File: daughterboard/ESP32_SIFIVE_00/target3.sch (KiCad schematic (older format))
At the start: 21 parts, among them IC2 W25X40CLSNIG, U3 ESP32-C3

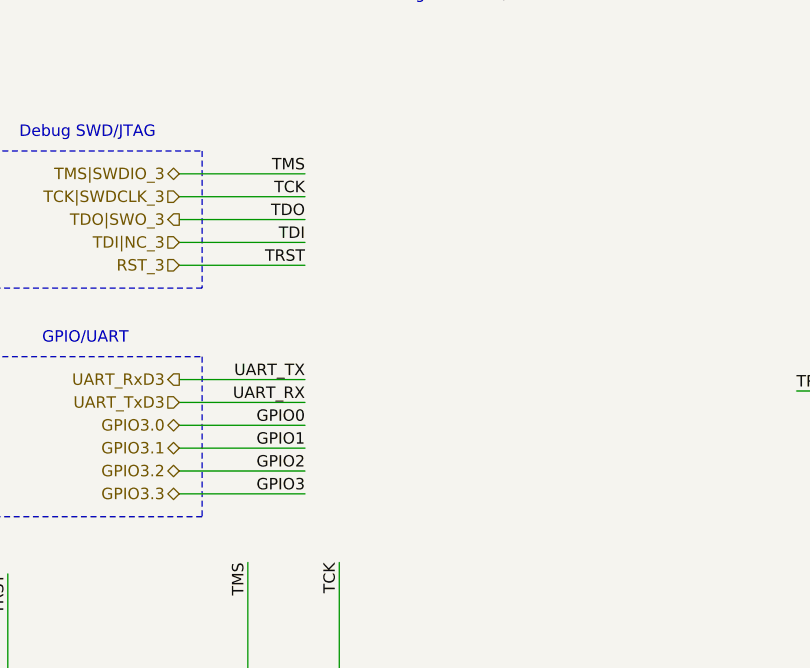
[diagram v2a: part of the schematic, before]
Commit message: added testpoints to daughterboards, updated readme
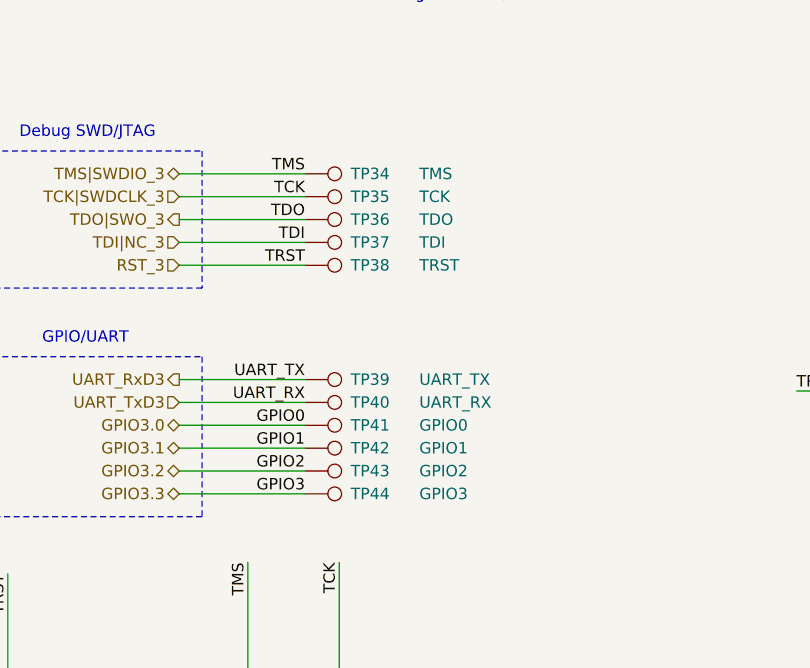
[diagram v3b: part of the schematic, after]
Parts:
- added TP34: TMS, symbol Connector:TestPoint
- added TP35: TCK, symbol Connector:TestPoint
- added TP36: TDO, symbol Connector:TestPoint
- added TP37: TDI, symbol Connector:TestPoint
- added TP38: TRST, symbol Connector:TestPoint
- added TP39: UART_TX, symbol Connector:TestPoint
- added TP40: UART_RX, symbol Connector:TestPoint
- added TP41: GPIO0, symbol Connector:TestPoint
- added TP42: GPIO1, symbol Connector:TestPoint
- added TP43: GPIO2, symbol Connector:TestPoint
- added TP44: GPIO3, symbol Connector:TestPoint
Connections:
- net GPIO3.0: now also TP41.1
- net GPIO3.1: now also TP42.1
- net GPIO3.2: now also TP43.1
- net GPIO3.3: now also TP44.1
- net RST_3: now also TP38.1
- net TCK|SWDCLK_3: now also TP35.1
- net TDI|NC_3: now also TP37.1
- net TDO|SWO_3: now also TP36.1
- net TMS|SWDIO_3: now also TP34.1
- net UART_RxD3: now also TP39.1
- net UART_TxD3: now also TP40.1
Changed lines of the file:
@@
+	0    1    1    0
+$EndComp
+$Comp
+L Connector:TestPoint TP?
+U 1 1 6191A87B
+P 2200 1700
+AR Path="/616688D6/6191A87B" Ref="TP?"  Part="1"
+AR Path="/61668157/6191A87B" Ref="TP34"  Part="1"
+F 0 "TP34" V 2200 1900 50  0000 L CNN
+F 1 "TMS" V 2200 2200 50  0000 L CNN
+F 2 "" H 2400 1700 50  0001 C CNN
+F 3 "~" H 2400 1700 50  0001 C CNN
+	1    2200 1700
+	0    1    1    0
+$EndComp
+$Comp
+L Connector:TestPoint TP?
+U 1 1 6191A881
+P 2200 1800
+AR Path="/616688D6/6191A881" Ref="TP?"  Part="1"
+AR Path="/61668157/6191A881" Ref="TP35"  Part="1"
+F 0 "TP35" V 2200 2000 50  0000 L CNN
+F 1 "TCK" V 2200 2300 50  0000 L CNN
+F 2 "" H 2400 1800 50  0001 C CNN
+F 3 "~" H 2400 1800 50  0001 C CNN
+	1    2200 1800
+	0    1    1    0
+$EndComp
+$Comp
+L Connector:TestPoint TP?
+U 1 1 6191A887
+P 2200 1900
+AR Path="/616688D6/6191A887" Ref="TP?"  Part="1"
+AR Path="/61668157/6191A887" Ref="TP36"  Part="1"
+F 0 "TP36" V 2200 2100 50  0000 L CNN
+F 1 "TDO" V 2200 2400 50  0000 L CNN
+F 2 "" H 2400 1900 50  0001 C CNN
+F 3 "~" H 2400 1900 50  0001 C CNN
+	1    2200 1900
+	0    1    1    0
+$EndComp
+$Comp
+L Connector:TestPoint TP?
+U 1 1 6191A88D
+P 2200 2000
+AR Path="/616688D6/6191A88D" Ref="TP?"  Part="1"
+AR Path="/61668157/6191A88D" Ref="TP37"  Part="1"
+F 0 "TP37" V 2200 2200 50  0000 L CNN
+F 1 "TDI" V 2200 2500 50  0000 L CNN
+F 2 "" H 2400 2000 50  0001 C CNN
+F 3 "~" H 2400 2000 50  0001 C CNN
+	1    2200 2000
+	0    1    1    0
+$EndComp
+$Comp
+L Connector:TestPoint TP?
+U 1 1 6191A893
+P 2200 2100
+AR Path="/616688D6/6191A893" Ref="TP?"  Part="1"
+AR Path="/61668157/6191A893" Ref="TP38"  Part="1"
+F 0 "TP38" V 2200 2300 50  0000 L CNN
+F 1 "TRST" V 2200 2600 50  0000 L CNN
+F 2 "" H 2400 2100 50  0001 C CNN
+F 3 "~" H 2400 2100 50  0001 C CNN
+	1    2200 2100
+	0    1    1    0
+$EndComp
+$Comp
+L Connector:TestPoint TP?
+U 1 1 6191A899
+P 2200 2600
+AR Path="/616688D6/6191A899" Ref="TP?"  Part="1"
+AR Path="/61668157/6191A899" Ref="TP39"  Part="1"
+F 0 "TP39" V 2200 2800 50  0000 L CNN
+F 1 "UART_TX" V 2200 3100 50  0000 L CNN
+F 2 "" H 2400 2600 50  0001 C CNN
+F 3 "~" H 2400 2600 50  0001 C CNN
+	1    2200 2600
+	0    1    1    0
+$EndComp
+$Comp
+L Connector:TestPoint TP?
+U 1 1 6191A89F
+P 2200 2700
+AR Path="/616688D6/6191A89F" Ref="TP?"  Part="1"
+AR Path="/61668157/6191A89F" Ref="TP40"  Part="1"
+F 0 "TP40" V 2200 2900 50  0000 L CNN
+F 1 "UART_RX" V 2200 3200 50  0000 L CNN
+F 2 "" H 2400 2700 50  0001 C CNN
+F 3 "~" H 2400 2700 50  0001 C CNN
+	1    2200 2700
+	0    1    1    0
+$EndComp
+$Comp
+L Connector:TestPoint TP?
+U 1 1 6191A8A5
+P 2200 2800
+AR Path="/616688D6/6191A8A5" Ref="TP?"  Part="1"
+AR Path="/61668157/6191A8A5" Ref="TP41"  Part="1"
+F 0 "TP41" V 2200 3000 50  0000 L CNN
+F 1 "GPIO0" V 2200 3300 50  0000 L CNN
+F 2 "" H 2400 2800 50  0001 C CNN
+F 3 "~" H 2400 2800 50  0001 C CNN
+	1    2200 2800
+	0    1    1    0
+$EndComp
+$Comp
+L Connector:TestPoint TP?
+U 1 1 6191A8AB
+P 2200 2900
+AR Path="/616688D6/6191A8AB" Ref="TP?"  Part="1"
+AR Path="/61668157/6191A8AB" Ref="TP42"  Part="1"
+F 0 "TP42" V 2200 3100 50  0000 L CNN
+F 1 "GPIO1" V 2200 3400 50  0000 L CNN
+F 2 "" H 2400 2900 50  0001 C CNN
+F 3 "~" H 2400 2900 50  0001 C CNN
+	1    2200 2900
+	0    1    1    0
+$EndComp
+$Comp
+L Connector:TestPoint TP?
+U 1 1 6191A8B1
+P 2200 3000
+AR Path="/616688D6/6191A8B1" Ref="TP?"  Part="1"
+AR Path="/61668157/6191A8B1" Ref="TP43"  Part="1"
+F 0 "TP43" V 2200 3200 50  0000 L CNN
+F 1 "GPIO2" V 2200 3500 50  0000 L CNN
+F 2 "" H 2400 3000 50  0001 C CNN
+F 3 "~" H 2400 3000 50  0001 C CNN
+	1    2200 3000
+	0    1    1    0
+$EndComp
+$Comp
+L Connector:TestPoint TP?
+U 1 1 6191A8B7
+P 2200 3100
+AR Path="/616688D6/6191A8B7" Ref="TP?"  Part="1"
+AR Path="/61668157/6191A8B7" Ref="TP44"  Part="1"
+F 0 "TP44" V 2200 3300 50  0000 L CNN
+F 1 "GPIO3" V 2200 3600 50  0000 L CNN
+F 2 "" H 2400 3100 50  0001 C CNN
+F 3 "~" H 2400 3100 50  0001 C CNN
+	1    2200 3100
 	0    1    1    0
 $EndComp

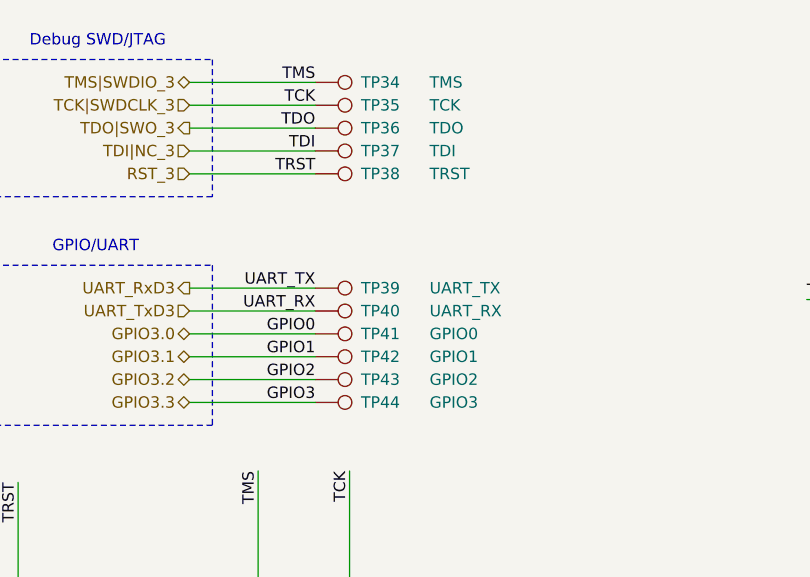
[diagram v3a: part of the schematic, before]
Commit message: started with esp32/sifive layout
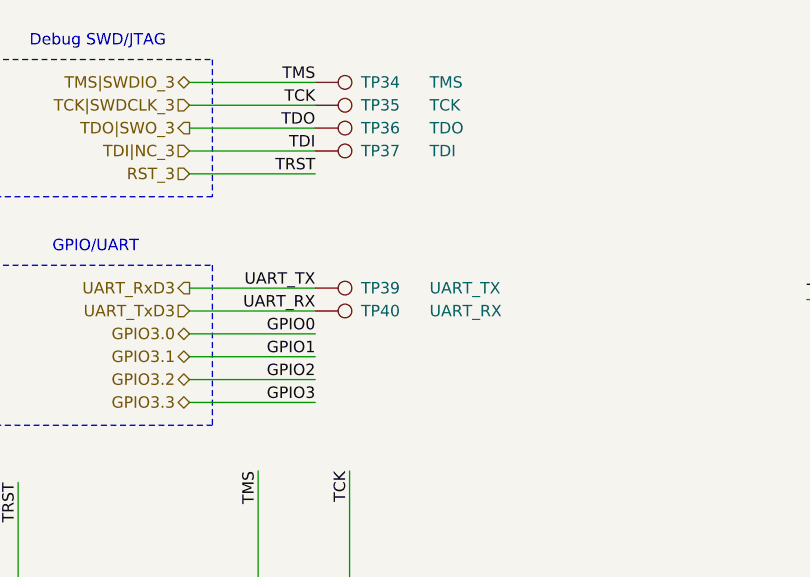
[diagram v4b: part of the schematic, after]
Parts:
- removed TP38: TRST, symbol Connector:TestPoint
- removed TP41: GPIO0, symbol Connector:TestPoint
- removed TP42: GPIO1, symbol Connector:TestPoint
- removed TP43: GPIO2, symbol Connector:TestPoint
- removed TP44: GPIO3, symbol Connector:TestPoint
- C16, C17, C18, C19, C20, C21, C22, C23, C24, C25: footprint (none) -> Capacitor_SMD:C_0603_1608Metric_Pad1.05x0.95mm_HandSolder
- JP4, JP5: footprint (none) -> Jumper:SolderJumper-2_P1.3mm_Open_TrianglePad1.0x1.5mm
- R13, R14, R15, R16, R17, R18, R19: footprint (none) -> Resistor_SMD:R_0603_1608Metric_Pad1.05x0.95mm_HandSolder
- TP34, TP35, TP36, TP37, TP39, TP40: footprint (none) -> TestPoint:TestPoint_Pad_1.0x1.0mm
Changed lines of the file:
@@
 F 0 "C17" H 4792 7046 50  0000 L CNN
 F 1 "1u" H 4792 6955 50  0000 L CNN
-F 2 "" H 4700 7000 50  0001 C CNN
+F 2 "Capacitor_SMD:C_0603_1608Metric_Pad1.05x0.95mm_HandSolder" H 4700 7000 50  0001 C CNN
 F 3 "~" H 4700 7000 50  0001 C CNN
 	1    4700 7000
@@
 F 0 "C18" H 5092 7046 50  0000 L CNN
 F 1 "100n" H 5092 6955 50  0000 L CNN
-F 2 "" H 5000 7000 50  0001 C CNN
+F 2 "Capacitor_SMD:C_0603_1608Metric_Pad1.05x0.95mm_HandSolder" H 5000 7000 50  0001 C CNN
 F 3 "~" H 5000 7000 50  0001 C CNN
 	1    5000 7000
@@
 F 0 "R16" H 5509 6796 50  0000 L CNN
 F 1 "10k" H 5509 6705 50  0000 L CNN
-F 2 "" H 5450 6750 50  0001 C CNN
+F 2 "Resistor_SMD:R_0603_1608Metric_Pad1.05x0.95mm_HandSolder" H 5450 6750 50  0001 C CNN
 F 3 "~" H 5450 6750 50  0001 C CNN
 	1    5450 6750
@@
 F 0 "C19" H 7092 1646 50  0000 L CNN
 F 1 "10u" H 7092 1555 50  0000 L CNN
-F 2 "" H 7000 1600 50  0001 C CNN
+F 2 "Capacitor_SMD:C_0603_1608Metric_Pad1.05x0.95mm_HandSolder" H 7000 1600 50  0001 C CNN
 F 3 "~" H 7000 1600 50  0001 C CNN
 	1    7000 1600
@@
 F 0 "C20" H 7492 1646 50  0000 L CNN
 F 1 "1u" H 7492 1555 50  0000 L CNN
-F 2 "" H 7400 1600 50  0001 C CNN
+F 2 "Capacitor_SMD:C_0603_1608Metric_Pad1.05x0.95mm_HandSolder" H 7400 1600 50  0001 C CNN
 F 3 "~" H 7400 1600 50  0001 C CNN
 	1    7400 1600
@@
 F 0 "C21" H 7842 1646 50  0000 L CNN
 F 1 "100n" H 7842 1555 50  0000 L CNN
-F 2 "" H 7750 1600 50  0001 C CNN
+F 2 "Capacitor_SMD:C_0603_1608Metric_Pad1.05x0.95mm_HandSolder" H 7750 1600 50  0001 C CNN
 F 3 "~" H 7750 1600 50  0001 C CNN
 	1    7750 1600
@@
 F 0 "C22" H 8242 1646 50  0000 L CNN
 F 1 "100n" H 8242 1555 50  0000 L CNN
-F 2 "" H 8150 1600 50  0001 C CNN
+F 2 "Capacitor_SMD:C_0603_1608Metric_Pad1.05x0.95mm_HandSolder" H 8150 1600 50  0001 C CNN
 F 3 "~" H 8150 1600 50  0001 C CNN
 	1    8150 1600
@@
 F 0 "C23" H 8642 1646 50  0000 L CNN
 F 1 "100n" H 8642 1555 50  0000 L CNN
-F 2 "" H 8550 1600 50  0001 C CNN
+F 2 "Capacitor_SMD:C_0603_1608Metric_Pad1.05x0.95mm_HandSolder" H 8550 1600 50  0001 C CNN
 F 3 "~" H 8550 1600 50  0001 C CNN
 	1    8550 1600
@@
 F 0 "C24" H 9042 1646 50  0000 L CNN
 F 1 "100n" H 9042 1555 50  0000 L CNN
-F 2 "" H 8950 1600 50  0001 C CNN
+F 2 "Capacitor_SMD:C_0603_1608Metric_Pad1.05x0.95mm_HandSolder" H 8950 1600 50  0001 C CNN
 F 3 "~" H 8950 1600 50  0001 C CNN
 	1    8950 1600
@@
 F 0 "C25" H 9442 1646 50  0000 L CNN
 F 1 "100n" H 9442 1555 50  0000 L CNN
-F 2 "" H 9350 1600 50  0001 C CNN
+F 2 "Capacitor_SMD:C_0603_1608Metric_Pad1.05x0.95mm_HandSolder" H 9350 1600 50  0001 C CNN
 F 3 "~" H 9350 1600 50  0001 C CNN
 	1    9350 1600
@@
 F 0 "R15" H 2409 4196 50  0000 L CNN
 F 1 "10k" H 2409 4105 50  0000 L CNN
-F 2 "" H 2350 4150 50  0001 C CNN
+F 2 "Resistor_SMD:R_0603_1608Metric_Pad1.05x0.95mm_HandSolder" H 2350 4150 50  0001 C CNN
 F 3 "~" H 2350 4150 50  0001 C CNN
 	1    2350 4150
@@
 F 0 "R14" H 2009 4196 50  0000 L CNN
 F 1 "10k" H 2009 4105 50  0000 L CNN
-F 2 "" H 1950 4150 50  0001 C CNN
+F 2 "Resistor_SMD:R_0603_1608Metric_Pad1.05x0.95mm_HandSolder" H 1950 4150 50  0001 C CNN
 F 3 "~" H 1950 4150 50  0001 C CNN
 	1    1950 4150
@@
 F 0 "R13" H 959 4196 50  0000 L CNN
 F 1 "100k" H 959 4105 50  0000 L CNN
-F 2 "" H 900 4150 50  0001 C CNN
+F 2 "Resistor_SMD:R_0603_1608Metric_Pad1.05x0.95mm_HandSolder" H 900 4150 50  0001 C CNN
 F 3 "~" H 900 4150 50  0001 C CNN
 	1    900  4150
@@
 F 0 "JP4" V 1554 4218 50  0000 L CNN
 F 1 "NRST" V 1645 4218 50  0000 L CNN
-F 2 "" H 1600 4150 50  0001 C CNN
+F 2 "Jumper:SolderJumper-2_P1.3mm_Open_TrianglePad1.0x1.5mm" H 1600 4150 50  0001 C CNN
 F 3 "~" H 1600 4150 50  0001 C CNN
 	1    1600 4150
@@
 F 0 "C16" H 1292 4196 50  0000 L CNN
 F 1 "100n" H 1292 4105 50  0000 L CNN
-F 2 "" H 1200 4150 50  0001 C CNN
+F 2 "Capacitor_SMD:C_0603_1608Metric_Pad1.05x0.95mm_HandSolder" H 1200 4150 50  0001 C CNN
 F 3 "~" H 1200 4150 50  0001 C CNN
 	1    1200 4150
@@
 F 0 "R17" V 7450 3600 50  0000 L CNN
 F 1 "100k" V 7450 4000 50  0000 L CNN
-F 2 "" H 7500 3850 50  0001 C CNN
+F 2 "Resistor_SMD:R_0603_1608Metric_Pad1.05x0.95mm_HandSolder" H 7500 3850 50  0001 C CNN
 F 3 "~" H 7500 3850 50  0001 C CNN
 	1    7500 3850
@@
 F 0 "R19" V 7450 3800 50  0000 L CNN
 F 1 "100k" V 7450 4200 50  0000 L CNN
-F 2 "" H 7500 4050 50  0001 C CNN
+F 2 "Resistor_SMD:R_0603_1608Metric_Pad1.05x0.95mm_HandSolder" H 7500 4050 50  0001 C CNN
 F 3 "~" H 7500 4050 50  0001 C CNN
 	1    7500 4050
@@
 F 0 "R18" V 7450 3700 50  0000 L CNN
 F 1 "100k" V 7450 4100 50  0000 L CNN
-F 2 "" H 7500 3950 50  0001 C CNN
+F 2 "Resistor_SMD:R_0603_1608Metric_Pad1.05x0.95mm_HandSolder" H 7500 3950 50  0001 C CNN
 F 3 "~" H 7500 3950 50  0001 C CNN
 	1    7500 3950
@@
 F 0 "JP5" H 9350 3075 50  0000 C CNN
 F 1 "BOOT" H 9350 3166 50  0000 C CNN
-F 2 "" H 9350 3300 50  0001 C CNN
+F 2 "Jumper:SolderJumper-2_P1.3mm_Open_TrianglePad1.0x1.5mm" H 9350 3300 50  0001 C CNN
 F 3 "~" H 9350 3300 50  0001 C CNN
 	1    9350 3300
@@
 F 0 "TP34" V 2200 1900 50  0000 L CNN
 F 1 "TMS" V 2200 2200 50  0000 L CNN
-F 2 "" H 2400 1700 50  0001 C CNN
+F 2 "TestPoint:TestPoint_Pad_1.0x1.0mm" H 2400 1700 50  0001 C CNN
 F 3 "~" H 2400 1700 50  0001 C CNN
 	1    2200 1700
@@
 F 0 "TP35" V 2200 2000 50  0000 L CNN
 F 1 "TCK" V 2200 2300 50  0000 L CNN
-F 2 "" H 2400 1800 50  0001 C CNN
+F 2 "TestPoint:TestPoint_Pad_1.0x1.0mm" H 2400 1800 50  0001 C CNN
 F 3 "~" H 2400 1800 50  0001 C CNN
 	1    2200 1800
@@
 F 0 "TP36" V 2200 2100 50  0000 L CNN
 F 1 "TDO" V 2200 2400 50  0000 L CNN
-F 2 "" H 2400 1900 50  0001 C CNN
+F 2 "TestPoint:TestPoint_Pad_1.0x1.0mm" H 2400 1900 50  0001 C CNN
 F 3 "~" H 2400 1900 50  0001 C CNN
 	1    2200 1900
@@
 F 0 "TP37" V 2200 2200 50  0000 L CNN
 F 1 "TDI" V 2200 2500 50  0000 L CNN
-F 2 "" H 2400 2000 50  0001 C CNN
+F 2 "TestPoint:TestPoint_Pad_1.0x1.0mm" H 2400 2000 50  0001 C CNN
 F 3 "~" H 2400 2000 50  0001 C CNN
 	1    2200 2000
-	0    1    1    0
-$EndComp
-$Comp
-L Connector:TestPoint TP?
-U 1 1 6191A893
-P 2200 2100
-AR Path="/616688D6/6191A893" Ref="TP?"  Part="1"
-AR Path="/61668157/6191A893" Ref="TP38"  Part="1"
-F 0 "TP38" V 2200 2300 50  0000 L CNN
-F 1 "TRST" V 2200 2600 50  0000 L CNN
-F 2 "" H 2400 2100 50  0001 C CNN
-F 3 "~" H 2400 2100 50  0001 C CNN
-	1    2200 2100
 	0    1    1    0
 $EndComp
@@
 F 0 "TP39" V 2200 2800 50  0000 L CNN
 F 1 "UART_TX" V 2200 3100 50  0000 L CNN
-F 2 "" H 2400 2600 50  0001 C CNN
+F 2 "TestPoint:TestPoint_Pad_1.0x1.0mm" H 2400 2600 50  0001 C CNN
 F 3 "~" H 2400 2600 50  0001 C CNN
 	1    2200 2600
@@
 F 0 "TP40" V 2200 2900 50  0000 L CNN
 F 1 "UART_RX" V 2200 3200 50  0000 L CNN
-F 2 "" H 2400 2700 50  0001 C CNN
+F 2 "TestPoint:TestPoint_Pad_1.0x1.0mm" H 2400 2700 50  0001 C CNN
 F 3 "~" H 2400 2700 50  0001 C CNN
 	1    2200 2700
 	0    1    1    0
 $EndComp
-$Comp
-L Connector:TestPoint TP?
-U 1 1 6191A8A5
-P 2200 2800
-AR Path="/616688D6/6191A8A5" Ref="TP?"  Part="1"
-AR Path="/61668157/6191A8A5" Ref="TP41"  Part="1"
-F 0 "TP41" V 2200 3000 50  0000 L CNN
-F 1 "GPIO0" V 2200 3300 50  0000 L CNN
-F 2 "" H 2400 2800 50  0001 C CNN
-F 3 "~" H 2400 2800 50  0001 C CNN
-	1    2200 2800
-	0    1    1    0
-$EndComp
-$Comp
-L Connector:TestPoint TP?
-U 1 1 6191A8AB
-P 2200 2900
-AR Path="/616688D6/6191A8AB" Ref="TP?"  Part="1"
-AR Path="/61668157/6191A8AB" Ref="TP42"  Part="1"
-F 0 "TP42" V 2200 3100 50  0000 L CNN
-F 1 "GPIO1" V 2200 3400 50  0000 L CNN
-F 2 "" H 2400 2900 50  0001 C CNN
-F 3 "~" H 2400 2900 50  0001 C CNN
-	1    2200 2900
-	0    1    1    0
-$EndComp
-$Comp
-L Connector:TestPoint TP?
-U 1 1 6191A8B1
-P 2200 3000
-AR Path="/616688D6/6191A8B1" Ref="TP?"  Part="1"
-AR Path="/61668157/6191A8B1" Ref="TP43"  Part="1"
-F 0 "TP43" V 2200 3200 50  0000 L CNN
-F 1 "GPIO2" V 2200 3500 50  0000 L CNN
-F 2 "" H 2400 3000 50  0001 C CNN
-F 3 "~" H 2400 3000 50  0001 C CNN
-	1    2200 3000
-	0    1    1    0
-$EndComp
-$Comp
-L Connector:TestPoint TP?
-U 1 1 6191A8B7
-P 2200 3100
-AR Path="/616688D6/6191A8B7" Ref="TP?"  Part="1"
-AR Path="/61668157/6191A8B7" Ref="TP44"  Part="1"
-F 0 "TP44" V 2200 3300 50  0000 L CNN
-F 1 "GPIO3" V 2200 3600 50  0000 L CNN
-F 2 "" H 2400 3100 50  0001 C CNN
-F 3 "~" H 2400 3100 50  0001 C CNN
-	1    2200 3100
-	0    1    1    0
-$EndComp
